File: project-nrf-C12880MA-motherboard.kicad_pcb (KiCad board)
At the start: 2 copper layers, 58.4 x 44.5 mm, 25 parts, among them IC1 TXU0204PWR, J1 Left, J2 Right, J3 PJ-036AH-SMT-TR, J4 SM04B-SRSS-TB(LF)(SN), J5 SM04B-SRSS-TB(LF)(SN), J6 SM04B-SRSS-TB(LF)(SN), J7 1702473, J8 C12880MA, U1 Opamp_Dual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

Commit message: Add version of previous commit
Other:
- board text added: "François Gervais 23 avril 2022 v1.0.0-6-g3728a19"
- board text removed: "François Gervais 23 avril 2022 v"
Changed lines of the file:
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@@
     (effects (font (size 1.5 1.5) (thickness 0.15)))
   )
-  (gr_text "François Gervais\n23 avril 2022\nv" (at 63.373 51.562) (layer B.SilkS)
+  (gr_text "François Gervais\n23 avril 2022\nv1.0.0-6-g3728a19" (at 63.373 51.562) (layer B.SilkS)
     (effects (font (size 1.5 1.5) (thickness 0.3)) (justify left mirror))
   )

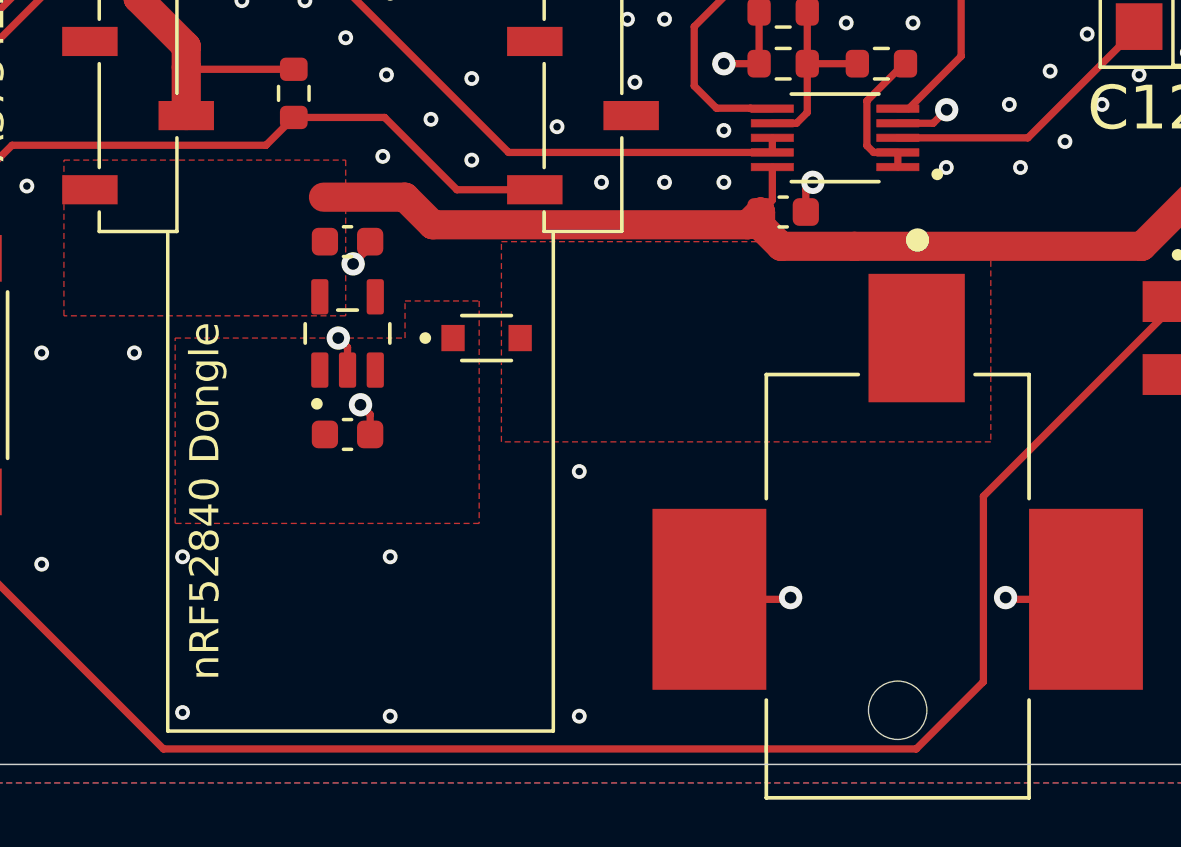
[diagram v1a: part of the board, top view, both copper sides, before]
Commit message: Reroute regulator section and fix cap footprint (0603->0805)
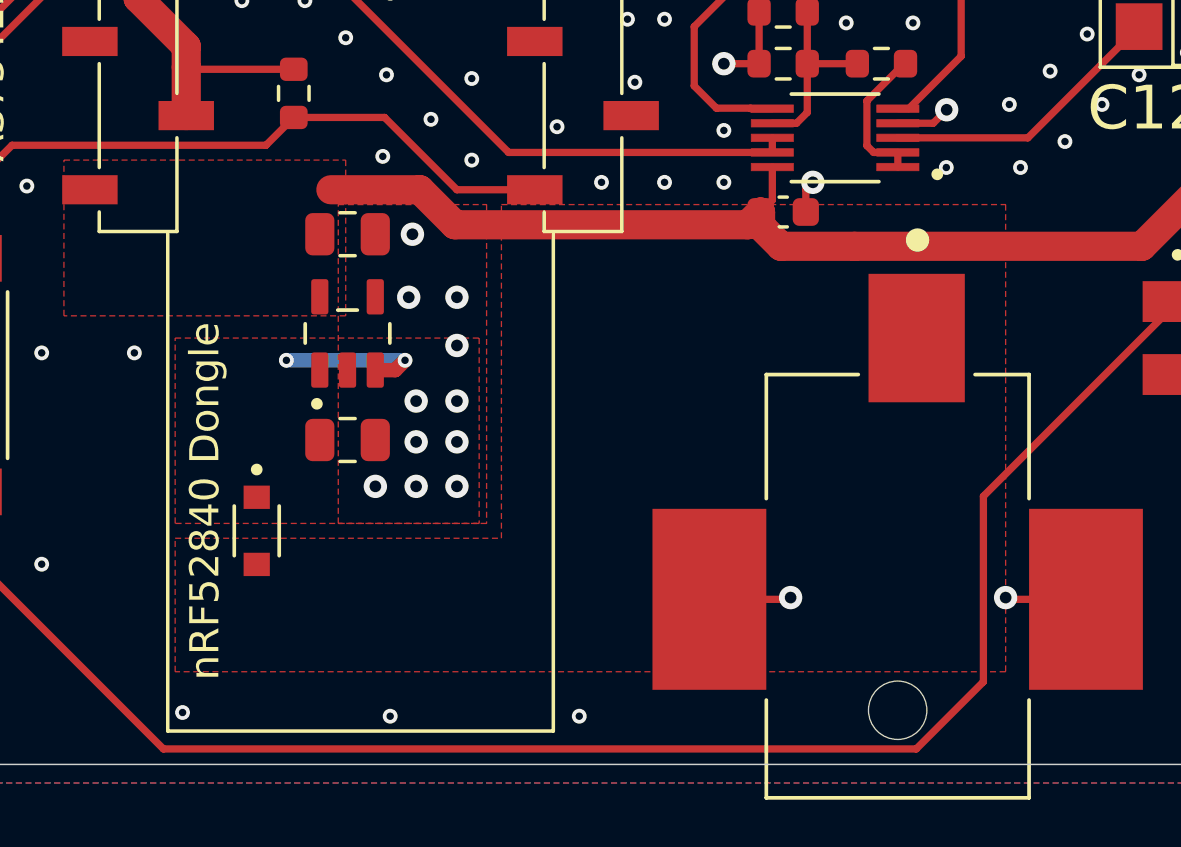
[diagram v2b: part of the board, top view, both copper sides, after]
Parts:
- C2, C3: footprint Capacitor_SMD:C_0603_1608Metric -> Capacitor_SMD:C_0805_2012Metric
- moved D1 10.3 mm to (30.7, 57.4), turned to 270 degrees
- moved C3 0.25 mm to (33.8, 47.2)
- moved C2 0.19 mm to (33.8, 54.3)
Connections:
- U2 pad 4: (no net) -> GND
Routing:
- net VCC: track 0.00 -> 5.22 mm, vias 0 -> 2
- net GND: track 45.4 -> 42.0 mm, vias 137 -> 142

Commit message: Add version of previous commit
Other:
- board text added: "François Gervais 23 avril 2022 v1.0.0-10-gc512b35"
- board text removed: "François Gervais 23 avril 2022 v1.0.0-6-g3728a19"
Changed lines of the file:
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@@
     (effects (font (size 1.5 1.5) (thickness 0.15)))
   )
-  (gr_text "François Gervais\n23 avril 2022\nv1.0.0-6-g3728a19" (at 63.373 51.562) (layer B.SilkS)
+  (gr_text "François Gervais\n23 avril 2022\nv1.0.0-10-gc512b35" (at 63.373 51.562) (layer B.SilkS)
     (effects (font (size 1.5 1.5) (thickness 0.3)) (justify left mirror))
   )

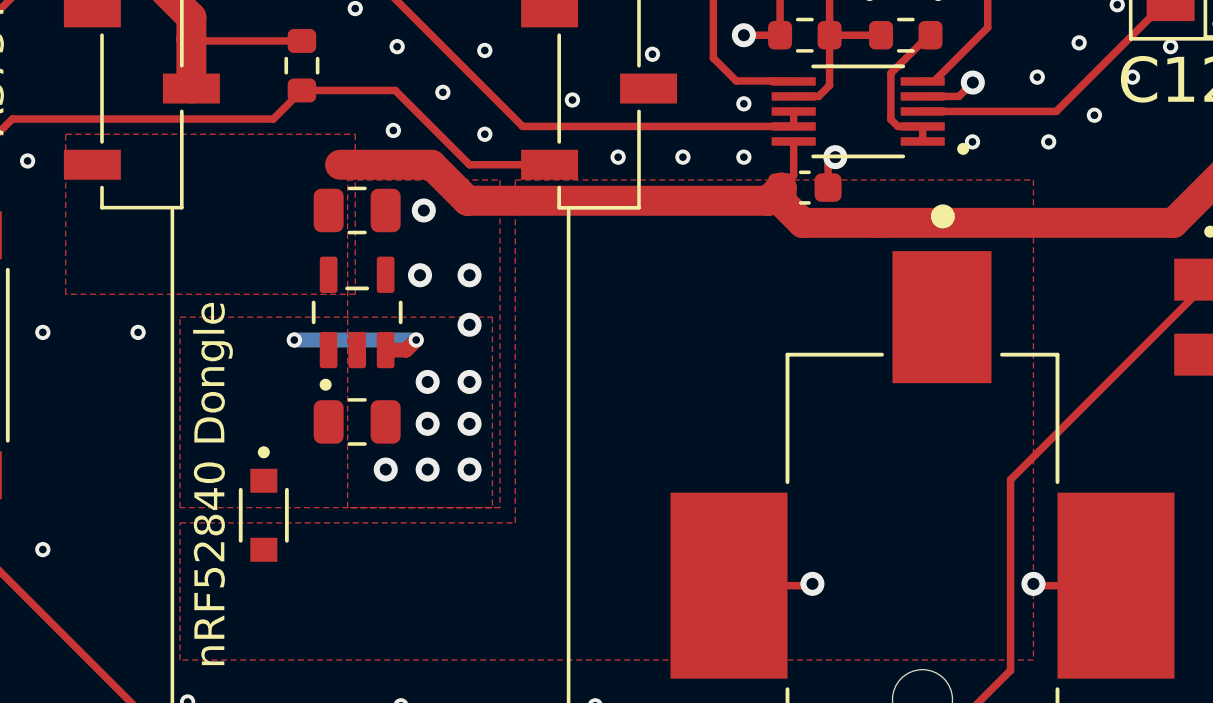
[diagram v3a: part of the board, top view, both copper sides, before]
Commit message: Swap the regulator for the LP2985-50
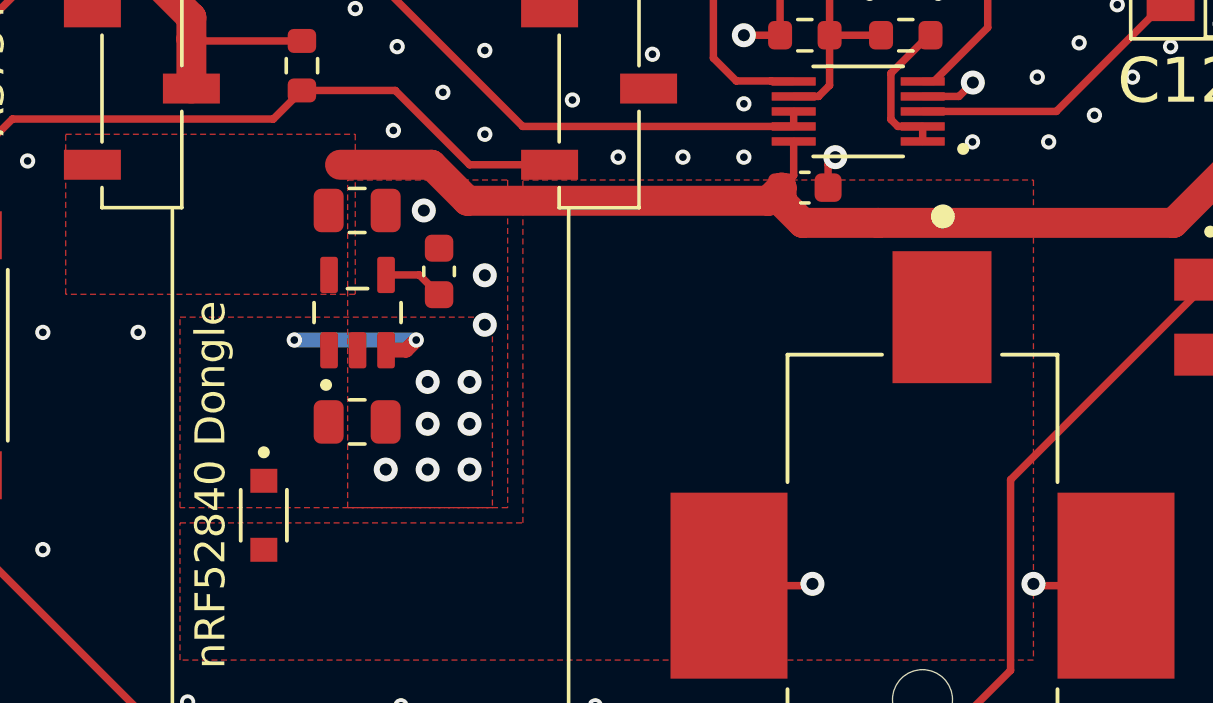
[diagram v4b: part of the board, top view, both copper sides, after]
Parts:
- added C1: 10nF, Capacitor_SMD:C_0603_1608Metric, F.Cu at (36.6, 49.3)
- U2: value TPS7A0350PDBVR -> LP2985-50DBVR; footprint TPS7A0233PDBVR:SOT95P280X145-5N -> LP2985-50:SOT95P280X145-5N
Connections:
- U2 pad 4: GND -> Net-(C1-Pad1)
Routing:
- net Net-(C1-Pad1): track 0.00 -> 2.04 mm
- net GND: vias 142 -> 141
